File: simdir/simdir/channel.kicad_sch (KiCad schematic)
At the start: 84 parts, among them J1 Conn_Coaxial, Q1 BC847, Q10 BC847, Q11 BC847, Q12 BC847, Q13 BC847, Q14 BC847, Q15 BC847, Q16 BC847, Q2 BC847, Q3 BC847, Q4 BC847, Q5 BC847, Q6 BC847, Q7 BC847, Q8 BC847, Q9 BC847, U1 MASWSS0178, U10 MASWSS0178, U11 MASWSS0178, U12 MASWSS0178, U13 MASWSS0178, U14 MASWSS0178, U15 MASWSS0178, U16 MASWSS0178, U17 LTV-847S, U18 LTV-847S, U19 74HCT595, U2 MASWSS0178, U3 MASWSS0178, U4 MASWSS0178, U5 MASWSS0178, U6 MASWSS0178, U7 MASWSS0178, U8 MASWSS0178, U9 MASWSS0178

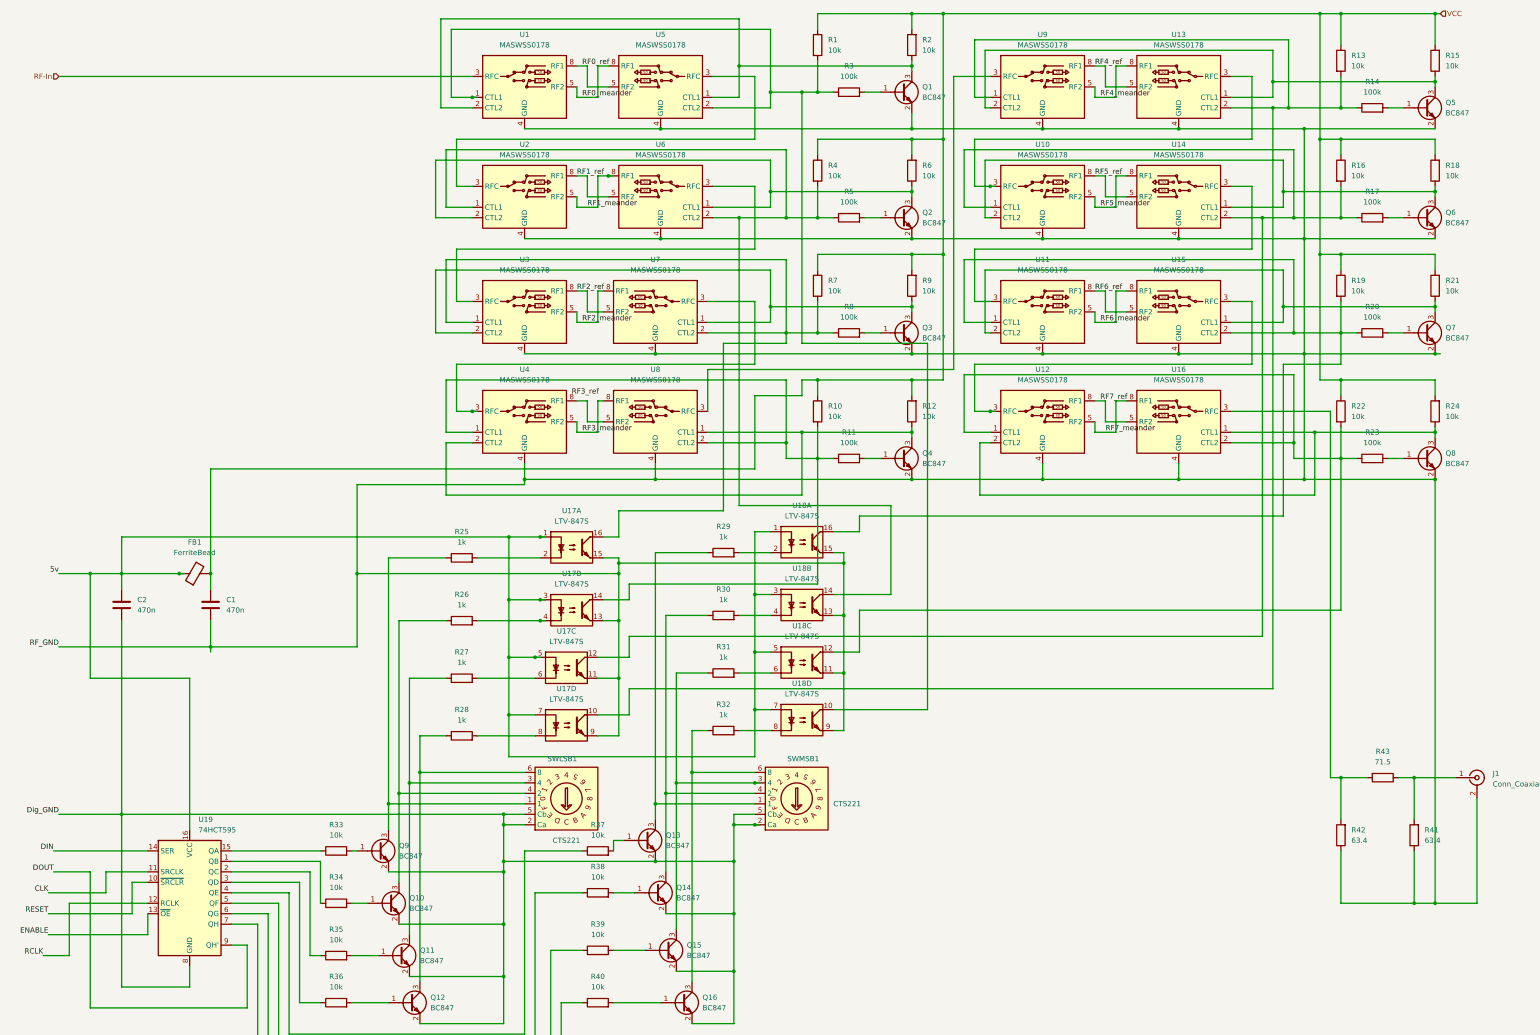
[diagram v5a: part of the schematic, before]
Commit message: Fixed minor issues with channel pins.
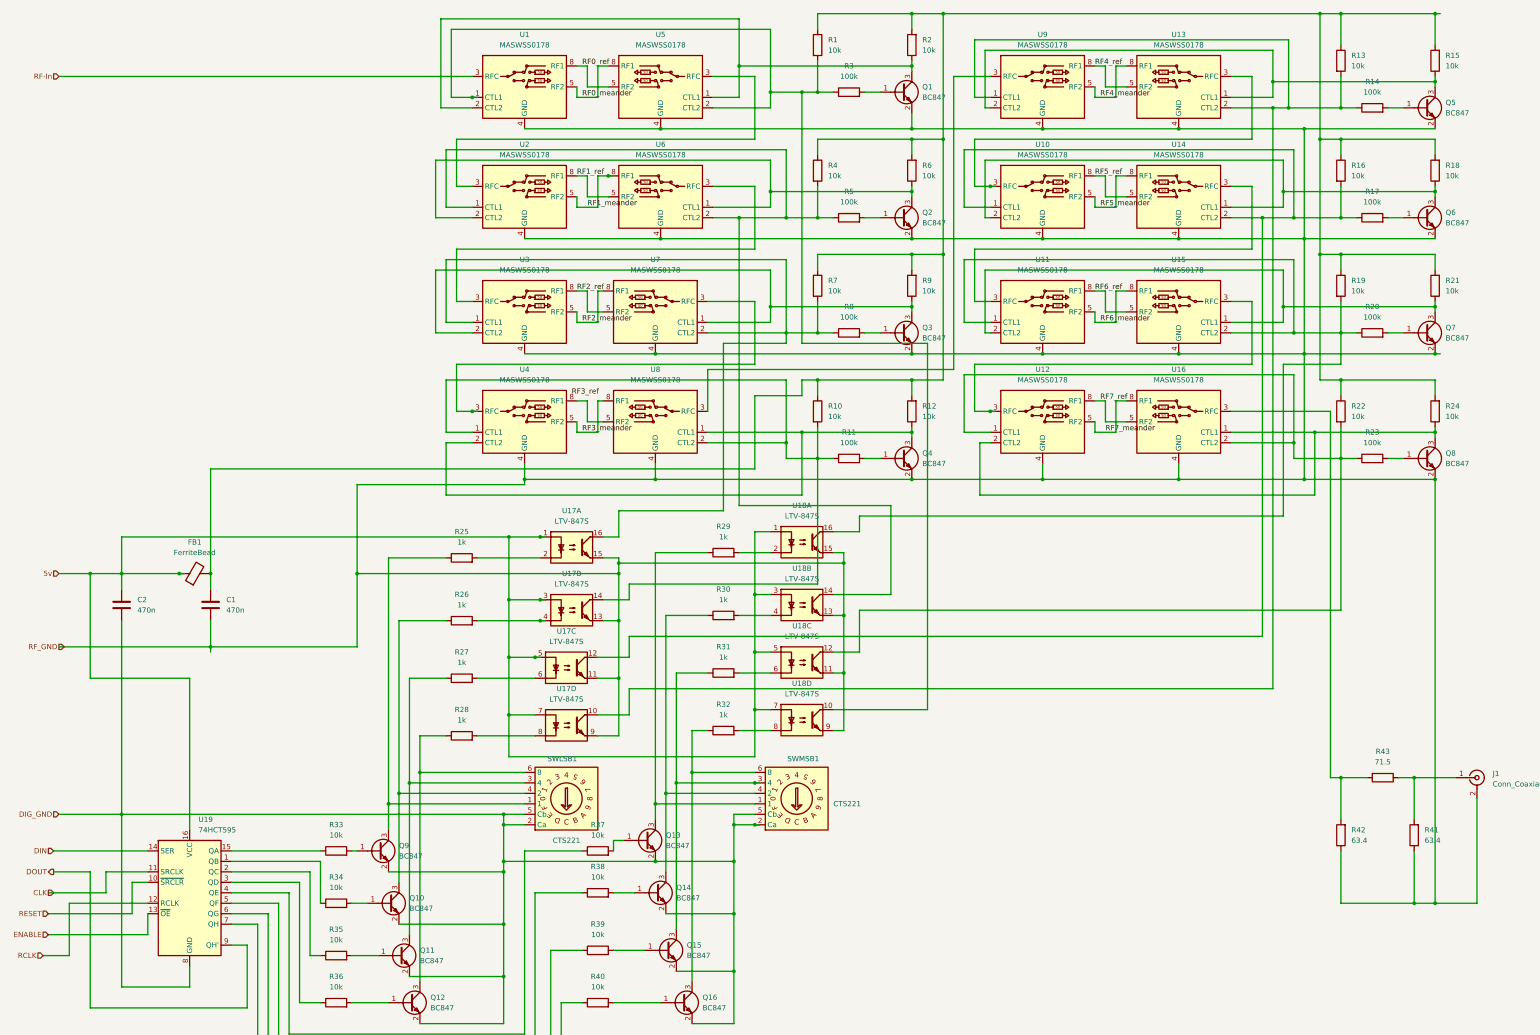
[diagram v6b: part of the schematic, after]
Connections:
- net Dig_GND renamed DIG_GND
- net VCC: no longer names the net of C1.1, FB1.2, R1.1, R10.1, R12.2, R13.1, R15.2, R16.1, R18.2, R19.1, R2.2, R21.2, R22.1, R24.2, R4.1, R6.2, R7.1, R9.2
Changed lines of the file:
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@@
-		)
-	)
-	(label "DIN"
-		(at 24.13 224.79 180)
-		(effects
-			(font
-				(size 1.27 1.27)
-			)
-			(justify right bottom)
-		)
-	)
-	(label "RCLK"
-		(at 21.59 250.19 180)
-		(effects
-			(font
-				(size 1.27 1.27)
-			)
-			(justify right bottom)
 		)
 	)
@@
 		)
 	)
-	(label "ENABLE"
-		(at 22.86 245.11 180)
-		(effects
-			(font
-				(size 1.27 1.27)
-			)
-			(justify right bottom)
-		)
-	)
 	(label "RF5_ref"
 		(at 276.86 60.96 0)
@@
 		)
 	)
-	(label "Dig_GND"
-		(at 25.4 215.9 180)
-		(effects
-			(font
-				(size 1.27 1.27)
-			)
-			(justify right bottom)
-		)
-	)
-	(label "DOUT"
-		(at 24.13 229.87 180)
-		(effects
-			(font
-				(size 1.27 1.27)
-			)
-			(justify right bottom)
-		)
-	)
 	(label "RF7_ref"
 		(at 278.13 115.57 0)
@@
 		)
 	)
-	(label "RESET"
-		(at 22.86 240.03 180)
-		(effects
-			(font
-				(size 1.27 1.27)
-			)
-			(justify right bottom)
-		)
-	)
 	(label "RF0_meander"
 		(at 152.4 41.91 0)
@@
 		)
 	)
-	(label "5v"
-		(at 25.4 157.48 180)
-		(effects
-			(font
-				(size 1.27 1.27)
-			)
-			(justify right bottom)
-		)
-	)
 	(label "RF6_meander"
 		(at 278.13 96.52 0)
@@
 		)
 	)
-	(label "CLK"
-		(at 22.86 234.95 180)
-		(effects
-			(font
-				(size 1.27 1.27)
-			)
-			(justify right bottom)
-		)
-	)
-	(label "RF_GND"
-		(at 25.4 175.26 180)
-		(effects
-			(font
-				(size 1.27 1.27)
-			)
-			(justify right bottom)
-		)
-	)
 	(label "RF5_meander"
 		(at 278.13 68.58 0)
@@
 		)
 	)
-	(hierarchical_label "VCC"
-		(shape input)
-		(at 360.68 21.59 0)
-		(effects
-			(font
-				(size 1.27 1.27)
-			)
-			(justify left)
-		)
-	)
+	(hierarchical_label "RCLK"
+		(shape input)
+		(at 21.59 250.19 180)
+		(effects
+			(font
+				(size 1.27 1.27)
+			)
+			(justify right)
+		)
+	)
+	(hierarchical_label "ENABLE"
+		(shape input)
+		(at 22.86 245.11 180)
+		(effects
+			(font
+				(size 1.27 1.27)
+			)
+			(justify right)
+		)
+	)
+	(hierarchical_label "DOUT"
+		(shape output)
+		(at 24.13 229.87 180)
+		(effects
+			(font
+				(size 1.27 1.27)
+			)
+			(justify right)
+		)
+	)
+	(hierarchical_label "RF_GND"
+		(shape input)
+		(at 26.67 175.26 180)
+		(effects
+			(font
+				(size 1.27 1.27)
+			)
+			(justify right)
+		)
+	)
+	(hierarchical_label "DIG_GND"
+		(shape input)
+		(at 25.4 215.9 180)
+		(effects
+			(font
+				(size 1.27 1.27)
+			)
+			(justify right)
+		)
+	)
+	(hierarchical_label "5v"
+		(shape input)
+		(at 25.4 157.48 180)
+		(effects
+			(font
+				(size 1.27 1.27)
+			)
+			(justify right)
+		)
+	)
+	(hierarchical_label "DIN"
+		(shape input)
+		(at 24.13 224.79 180)
+		(effects
+			(font
+				(size 1.27 1.27)
+			)
+			(justify right)
+		)
+	)
+	(hierarchical_label "CLK"
+		(shape input)
+		(at 24.13 234.95 180)
+		(effects
+			(font
+				(size 1.27 1.27)
+			)
+			(justify right)
+		)
+	)
+	(hierarchical_label "RESET"
+		(shape input)
+		(at 22.86 240.03 180)
+		(effects
+			(font
+				(size 1.27 1.27)
+			)
+			(justify right)
+		)
+	)

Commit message: Fixed layout issues & added splitter.
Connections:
- net RF-In: now also U16.3 (RFC); no longer U1.3 (RFC)
- net at R42.2, R43.2: now also J1.1 (In); no longer U16.3 (RFC)
- net at R41.2, R43.1: now also U1.3 (RFC); no longer J1.1 (In)
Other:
- moved on the sheet: J1, R41, R42, R43
